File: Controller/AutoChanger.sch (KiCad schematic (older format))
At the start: 37 parts, among them J1 OLED, P10 SENSOR, P11 SENSOR, P12 LOGO, P13 5, P3 1, P4 2, P5 3, P6 4, P7 6, P8 M3, P9 M3, SW1 RESET, SW2 1, SW3 2, SW4 3, SW5 4, SW6 PRGM, U1 arduino_nano, U3 ITR9606-F

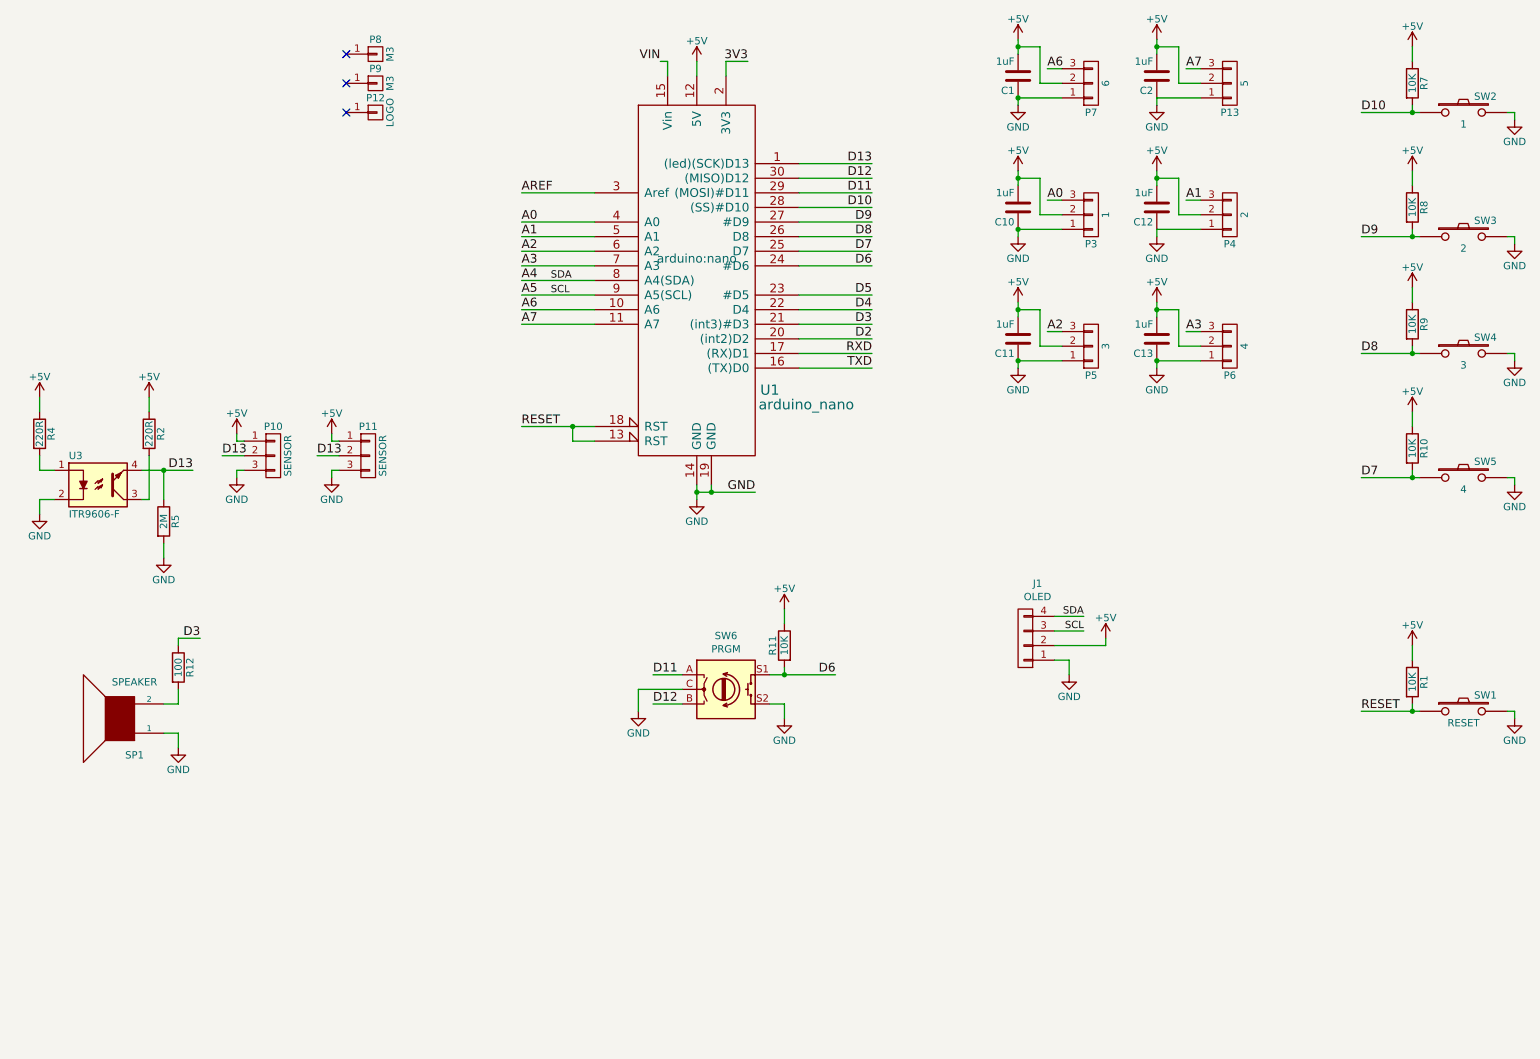
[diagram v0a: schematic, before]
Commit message: Tinypico compatible controller
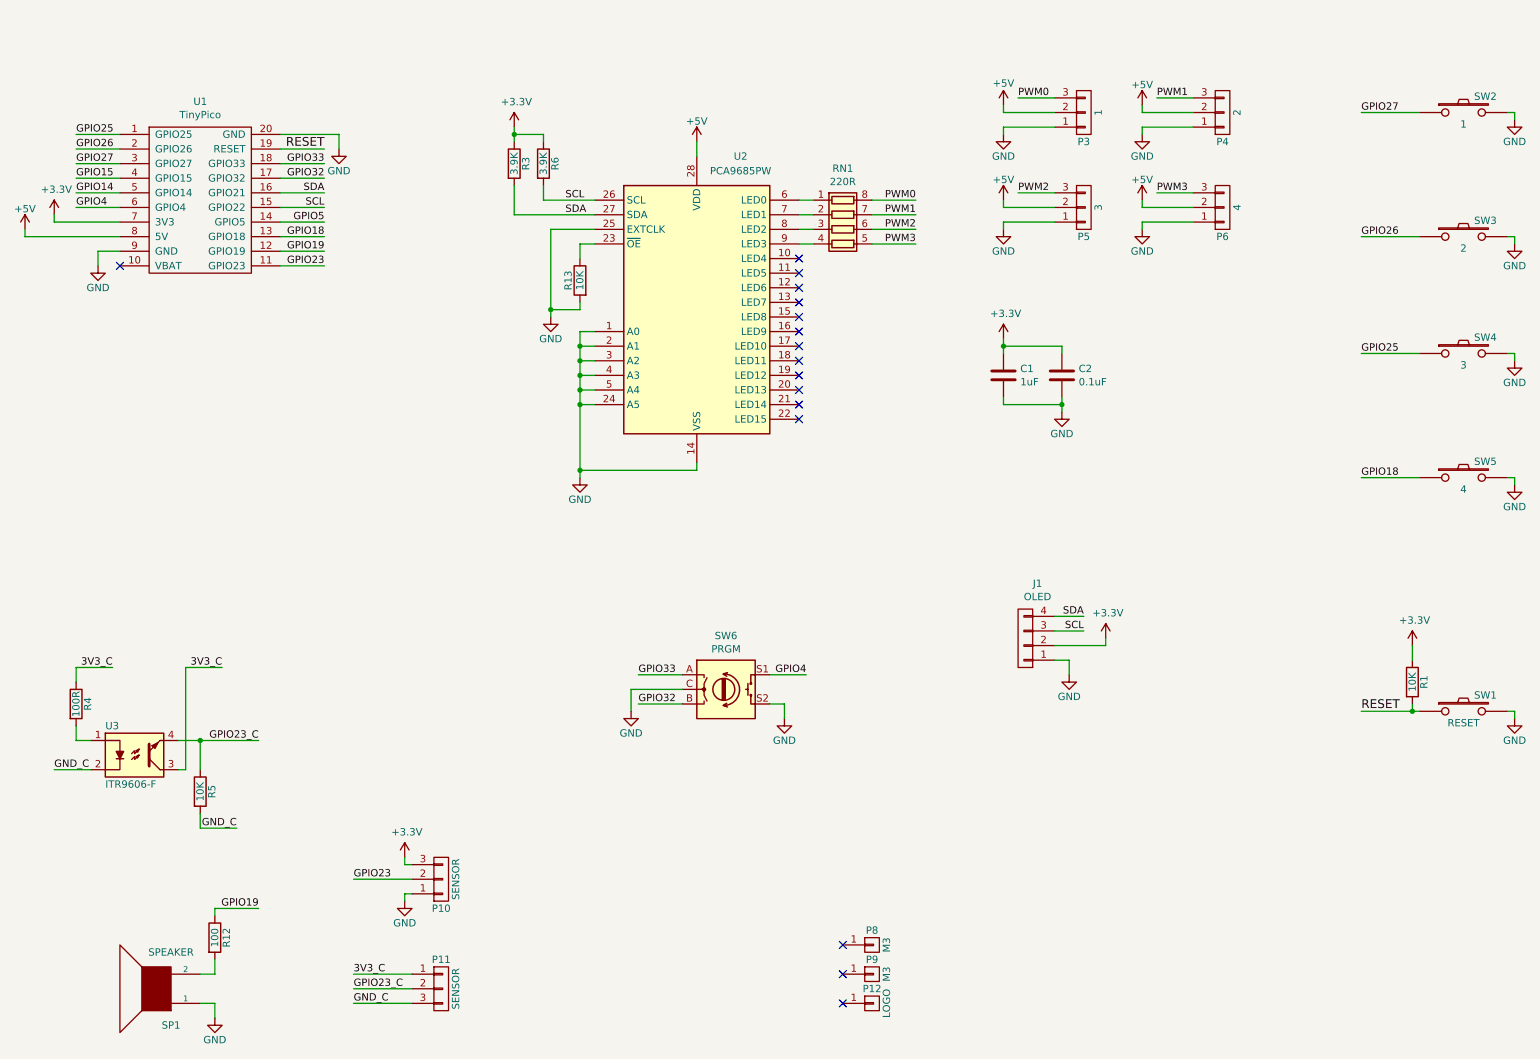
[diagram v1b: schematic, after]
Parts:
- removed C10, C11, C12, C13: 1uF, Capacitors_SMD:C_0603_HandSoldering, symbol Device:C
- removed P13: 5, Pin_Headers:Pin_Header_Straight_1x03_Pitch2.54mm, symbol AutoChanger-rescue:CONN_01X03
- removed P7: 6, Pin_Headers:Pin_Header_Straight_1x03_Pitch2.54mm, symbol AutoChanger-rescue:CONN_01X03
- removed R10, R11, R7, R8, R9: 10K, Resistors_SMD:R_0603_HandSoldering, symbol Device:R
- removed R2: 220R, Resistors_SMD:R_0603_HandSoldering, symbol Device:R
- removed U1: arduino_nano, arduino:nano, symbol arduino:arduino_nano
- added R13: 10K, Resistor_SMD:R_0603_1608Metric_Pad1.05x0.95mm_HandSolder, symbol Device:R
- added R3, R6: 3.9K, Resistor_SMD:R_0603_1608Metric_Pad1.05x0.95mm_HandSolder, symbol Device:R
- added RN1: 220R, Resistor_SMD:R_Array_Concave_4x0603, symbol Device:R_Pack04
- added U1: TinyPico, libs:TinyPico, symbol tinypico:TinyPico
- added U2: PCA9685PW, Package_SO:TSSOP-28_4.4x9.7mm_P0.65mm, symbol Driver_LED:PCA9685PW
- C1: footprint Capacitors_SMD:C_0603_HandSoldering -> Capacitor_SMD:C_0603_1608Metric_Pad1.05x0.95mm_HandSolder
- C2: value 1uF -> 0.1uF; footprint Capacitors_SMD:C_0603_HandSoldering -> Capacitor_SMD:C_0603_1608Metric_Pad1.05x0.95mm_HandSolder
- R4: value 220R -> 100R
- R5: value 2M -> 10K
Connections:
- net +5V: now also U1.8 (5V), U2.28 (VDD); no longer C1.2, C2.2, J1.2 (P2), P10.1 (P1), P11.1 (P1), R1.1, R4.1
- net GND: now also C1.2, C2.2, P10.1 (P1), R13.2, U1.20 (GND), U1.9 (GND), U2.1 (A0), U2.14 (VSS), U2.2 (A1), U2.24 (A5), U2.25 (EXTCLK), U2.3 (A2), U2.4 (A3), U2.5 (A4); no longer C1.1, C2.1, P10.3 (P3), P11.3 (P3), R5.2, U3.2
- net RESET: now also U1.19 (RESET)
- net 3V3_C: now reaches U3.3
- net 3V3_C: now also P11.1 (P1), R4.1
- net A0 renamed PWM0
- net PWM0: now also RN1.8 (R1.2)
- net A1 renamed PWM1
- net PWM1: now also RN1.7 (R2.2)
- net A2 renamed PWM2
- net PWM2: now also RN1.6 (R3.2)
- net A3 renamed PWM3
- net PWM3: now also RN1.5 (R4.2)
- net A4 renamed SDA
- net SDA: now also R3.2, U1.16 (GPIO21), U2.27 (SDA)
- net A5 renamed SCL
- net SCL: now also R6.2, U1.15 (GPIO22), U2.26 (SCL)
- net D10 renamed GPIO27
- net GPIO27: now also U1.3 (GPIO27)
- net D11 renamed GPIO33
- net GPIO33: now also U1.18 (GPIO33)
- net D12 renamed GPIO32
- net GPIO32: now also U1.17 (GPIO32)
- net D13 renamed GPIO23_C
- net GPIO23_C: no longer P10.2 (P2)
- net D3 renamed GPIO19
- net GPIO19: now also U1.12 (GPIO19)
- net D6 renamed GPIO4
- net GPIO4: now also U1.6 (GPIO4)
- net D7 renamed GPIO18
- net GPIO18: now also U1.13 (GPIO18)
- net D8 renamed GPIO25
- net GPIO25: now also U1.1 (GPIO25)
- net D9 renamed GPIO26
- net GPIO26: now also U1.2 (GPIO26)
- new net: R13.1, U2.23 (~OE)
- new net: RN1.1 (R1.1), U2.6 (LED0)
- new net: RN1.2 (R2.1), U2.7 (LED1)
- new net: RN1.3 (R3.1), U2.8 (LED2)
- new net: RN1.4 (R4.1), U2.9 (LED3)
- new net +3V3: C1.1, C2.1, J1.2 (P2), P10.3 (P3), R1.1, R3.1, R6.1, U1.7 (3V3)
- new net GND_C: P11.3 (P3), R5.2, U3.2
- new net GPIO14: U1.5 (GPIO14)
- new net GPIO15: U1.4 (GPIO15)
- new net GPIO23: P10.2 (P2), U1.11 (GPIO23)
- new net GPIO5: U1.14 (GPIO5)
- no-connect marks 3 -> 16
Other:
- moved on the sheet: P10, P11, P12, P3, P4, P5, P6, P8, P9, R12, R4, R5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
